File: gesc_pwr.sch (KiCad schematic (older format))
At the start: 45 parts, among them J10 PHASE_C, J11 PHASE_B, J12 NTC, J9 PHASE_A, Q1 TPH2R608NH,L1Q, Q2 TPH2R608NH,L1Q, Q3 TPH2R608NH,L1Q, Q4 TPH2R608NH,L1Q, Q5 TPH2R608NH,L1Q, Q6 TPH2R608NH,L1Q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

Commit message: save
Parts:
- J10, J11, J9: footprint gsvesc:TestPoint_Pad_5.0x5.0mm -> gesc:TestPoint_Pad_5.0x5.0mm
- J12: footprint gsvesc:2pad_smd_testpin -> gesc:2pad_smd_testpin
- Q1, Q2, Q4, Q5, Q6: footprint gsvesc:TRANS_TPHR8504PL-3PIN -> gesc:TRANS_TPHR8504PL-3PIN; symbol gsvesc:TPH2R506PL -> gesc:TPH2R506PL
- Q3: footprint gsvesc:TRANS_TPHR8504PL-3PIN -> gesc:TRANS_TPHR8504PL-3PIN; symbol gsvesc:TPH2R608NH -> gesc:TPH2R608NH
- U4, U5, U6: footprint gsvesc:INA240A1QPWRQ1 -> gesc:INA240A1QPWRQ1; symbol gsvesc:INA240A3 -> gesc:INA240A3
- U7, U8, U9: footprint gsvesc:M74VHC1GT66DTT1G -> gesc:M74VHC1GT66DTT1G; symbol gsvesc:M74VHC1GT66DTT1G -> gesc:M74VHC1GT66DTT1G
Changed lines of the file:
@@
 encoding utf-8
 Sheet 5 5
-Title "GSESC - DC Motor Controler"
-Date "2018-11-11"
-Rev "4.0"
+Title "GESC - DC Motor Controler"
+Date "2020-04-09"
+Rev "6.0"
 Comp ""
 Comment1 ""
@@
 F 0 "J10" H 4130 1642 50  0000 L CNN
 F 1 "PHASE_C" H 4130 1551 50  0000 L CNN
-F 2 "gsvesc:TestPoint_Pad_5.0x5.0mm" H 4050 1600 50  0001 C CNN
+F 2 "gesc:TestPoint_Pad_5.0x5.0mm" H 4050 1600 50  0001 C CNN
 F 3 "~" H 4050 1600 50  0001 C CNN
 	1    4050 1600
@@
 F 0 "J12" V 10054 1430 50  0000 L CNN
 F 1 "NTC" V 10145 1430 50  0000 L CNN
-F 2 "gsvesc:2pad_smd_testpin" H 10050 1350 50  0001 C CNN
+F 2 "gesc:2pad_smd_testpin" H 10050 1350 50  0001 C CNN
 F 3 "~" H 10050 1350 50  0001 C CNN
 	1    10050 1350
@@
 PHASE_C
 $Comp
-L gsvesc:M74VHC1GT66DTT1G U7
+L gesc:M74VHC1GT66DTT1G U7
 U 1 1 5DF40CC9
 P 6250 5450
 F 0 "U7" H 6900 5937 60  0000 C CNN
 F 1 "SN74LVC1G66DBVR" H 6900 5831 60  0000 C CNN
-F 2 "gsvesc:M74VHC1GT66DTT1G" H 6750 5250 60  0001 C CNN
+F 2 "gesc:M74VHC1GT66DTT1G" H 6750 5250 60  0001 C CNN
 F 3 "" H 6250 5450 60  0000 C CNN
 	1    6250 5450
@@
 CURR_B
 $Comp
-L gsvesc:M74VHC1GT66DTT1G U8
+L gesc:M74VHC1GT66DTT1G U8
 U 1 1 5DF8119A
 P 6250 3700
 F 0 "U8" H 6900 4187 60  0000 C CNN
 F 1 "SN74LVC1G66DBVR" H 6900 4081 60  0000 C CNN
-F 2 "gsvesc:M74VHC1GT66DTT1G" H 6750 3500 60  0001 C CNN
+F 2 "gesc:M74VHC1GT66DTT1G" H 6750 3500 60  0001 C CNN
 F 3 "" H 6250 3700 60  0000 C CNN
 	1    6250 3700
@@
 CURR_C
 $Comp
-L gsvesc:M74VHC1GT66DTT1G U9
+L gesc:M74VHC1GT66DTT1G U9
 U 1 1 5DFA4855
 P 6250 1950
 F 0 "U9" H 6900 2437 60  0000 C CNN
 F 1 "SN74LVC1G66DBVR" H 6900 2331 60  0000 C CNN
-F 2 "gsvesc:M74VHC1GT66DTT1G" H 6750 1750 60  0001 C CNN
+F 2 "gesc:M74VHC1GT66DTT1G" H 6750 1750 60  0001 C CNN
 F 3 "" H 6250 1950 60  0000 C CNN
 	1    6250 1950
@@
 	6150 2000 6150 2050
 $Comp
-L gsvesc:TPH2R608NH Q3
+L gesc:TPH2R608NH Q3
 U 1 1 5E3D365F
 P 1650 1300
 F 0 "Q3" H 1550 1450 50  0000 L CNN
 F 1 "TPH2R608NH,L1Q" H 1250 1150 50  0000 L CNN
-F 2 "gsvesc:TRANS_TPHR8504PL-3PIN" H 1650 1300 50  0001 C CIN
+F 2 "gesc:TRANS_TPHR8504PL-3PIN" H 1650 1300 50  0001 C CIN
 F 3 "" H 1650 1300 50  0001 L CNN
 F 4 "C146377" H 0   0   50  0001 C CNN "LCSC"
@@
 $EndComp
 $Comp
-L gsvesc:TPH2R506PL Q4
+L gesc:TPH2R506PL Q4
 U 1 1 5E3D3778
 P 1650 1950
 F 0 "Q4" H 1600 2100 50  0000 L CNN
 F 1 "TPH2R608NH,L1Q" H 1200 1800 50  0000 L CNN
-F 2 "gsvesc:TRANS_TPHR8504PL-3PIN" H 1650 1950 50  0001 C CIN
+F 2 "gesc:TRANS_TPHR8504PL-3PIN" H 1650 1950 50  0001 C CIN
 F 3 "" H 1650 1950 50  0001 L CNN
 F 4 "C146377" H 0   0   50  0001 C CNN "LCSC"
@@
 	3550 1600 3550 2050
 $Comp
-L gsvesc:INA240A3 U5
+L gesc:INA240A3 U5
 U 1 1 5E579C2A
 P 4250 2450
 F 0 "U5" H 3975 3138 60  0000 C CNN
 F 1 "INA240A2" H 3975 3032 60  0000 C CNN
-F 2 "gsvesc:INA240A1QPWRQ1" H 4000 2400 60  0001 C CNN
+F 2 "gesc:INA240A1QPWRQ1" H 4000 2400 60  0001 C CNN
 F 3 "" H 4250 2450 60  0000 C CNN
 	1    4250 2450
@@
 F 0 "J11" H 4130 3842 50  0000 L CNN
 F 1 "PHASE_B" H 4130 3751 50  0000 L CNN
-F 2 "gsvesc:TestPoint_Pad_5.0x5.0mm" H 4050 3800 50  0001 C CNN
+F 2 "gesc:TestPoint_Pad_5.0x5.0mm" H 4050 3800 50  0001 C CNN
 F 3 "~" H 4050 3800 50  0001 C CNN
 	1    4050 3800
@@
 PHASE_B
 $Comp
-L gsvesc:TPH2R506PL Q5
+L gesc:TPH2R506PL Q5
 U 1 1 5E6023E2
 P 1650 3500
 F 0 "Q5" H 1550 3650 50  0000 L CNN
 F 1 "TPH2R608NH,L1Q" H 1250 3350 50  0000 L CNN
-F 2 "gsvesc:TRANS_TPHR8504PL-3PIN" H 1650 3500 50  0001 C CIN
+F 2 "gesc:TRANS_TPHR8504PL-3PIN" H 1650 3500 50  0001 C CIN
 F 3 "" H 1650 3500 50  0001 L CNN
 F 4 "C146377" H 0   0   50  0001 C CNN "LCSC"
@@
 $EndComp
 $Comp
-L gsvesc:TPH2R506PL Q6
+L gesc:TPH2R506PL Q6
 U 1 1 5E6023E8
 P 1650 4150
 F 0 "Q6" H 1600 4300 50  0000 L CNN
 F 1 "TPH2R608NH,L1Q" H 1200 4000 50  0000 L CNN
-F 2 "gsvesc:TRANS_TPHR8504PL-3PIN" H 1650 4150 50  0001 C CIN
+F 2 "gesc:TRANS_TPHR8504PL-3PIN" H 1650 4150 50  0001 C CIN
 F 3 "" H 1650 4150 50  0001 L CNN
 F 4 "C146377" H 0   0   50  0001 C CNN "LCSC"
@@
 	3550 3800 3550 4250
 $Comp
-L gsvesc:INA240A3 U6
+L gesc:INA240A3 U6
 U 1 1 5E60242D
 P 4250 4650
 F 0 "U6" H 3975 5338 60  0000 C CNN
 F 1 "INA240A2" H 3975 5232 60  0000 C CNN
-F 2 "gsvesc:INA240A1QPWRQ1" H 4000 4600 60  0001 C CNN
+F 2 "gesc:INA240A1QPWRQ1" H 4000 4600 60  0001 C CNN
 F 3 "" H 4250 4650 60  0000 C CNN
 	1    4250 4650
@@
 F 0 "J9" H 4030 6292 50  0000 L CNN
 F 1 "PHASE_A" H 4030 6201 50  0000 L CNN
-F 2 "gsvesc:TestPoint_Pad_5.0x5.0mm" H 3950 6250 50  0001 C CNN
+F 2 "gesc:TestPoint_Pad_5.0x5.0mm" H 3950 6250 50  0001 C CNN
 F 3 "~" H 3950 6250 50  0001 C CNN
 	1    3950 6250
@@
 PHASE_A
 $Comp
-L gsvesc:TPH2R506PL Q1
+L gesc:TPH2R506PL Q1
 U 1 1 5E60A8BA
 P 1600 5950
 F 0 "Q1" H 1500 6100 50  0000 L CNN
 F 1 "TPH2R608NH,L1Q" H 1200 5800 50  0000 L CNN
-F 2 "gsvesc:TRANS_TPHR8504PL-3PIN" H 1600 5950 50  0001 C CIN
+F 2 "gesc:TRANS_TPHR8504PL-3PIN" H 1600 5950 50  0001 C CIN
 F 3 "" H 1600 5950 50  0001 L CNN
 F 4 "C146377" H 0   0   50  0001 C CNN "LCSC"
@@
 $EndComp
 $Comp
-L gsvesc:TPH2R506PL Q2
+L gesc:TPH2R506PL Q2
 U 1 1 5E60A8C0
 P 1600 6600
 F 0 "Q2" H 1550 6750 50  0000 L CNN
 F 1 "TPH2R608NH,L1Q" H 1150 6450 50  0000 L CNN
-F 2 "gsvesc:TRANS_TPHR8504PL-3PIN" H 1600 6600 50  0001 C CIN
+F 2 "gesc:TRANS_TPHR8504PL-3PIN" H 1600 6600 50  0001 C CIN
 F 3 "" H 1600 6600 50  0001 L CNN
 F 4 "C146377" H 0   0   50  0001 C CNN "LCSC"
@@
 	3450 6250 3450 6700
 $Comp
-L gsvesc:INA240A3 U4
+L gesc:INA240A3 U4
 U 1 1 5E60A905
 P 4150 7100
 F 0 "U4" H 3875 7788 60  0000 C CNN
 F 1 "INA240A2" H 3875 7682 60  0000 C CNN
-F 2 "gsvesc:INA240A1QPWRQ1" H 3900 7050 60  0001 C CNN
+F 2 "gesc:INA240A1QPWRQ1" H 3900 7050 60  0001 C CNN
 F 3 "" H 4150 7100 60  0000 C CNN
 	1    4150 7100

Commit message: save
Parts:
- added C51, C52, C53, C55, C57, C58: 10u0/75V, Capacitor_SMD:C_1210_3225Metric, symbol Device:C
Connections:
- net GND: now also C51.2, C52.2, C53.2, C55.2, C57.2, C58.2
- net VBAT: now also C51.1, C52.1, C53.1, C55.1, C57.1, C58.1
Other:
- moved on the sheet: C45, C46, C48, J10, J11, J9, R31, R45, R46, U4, U5, U6

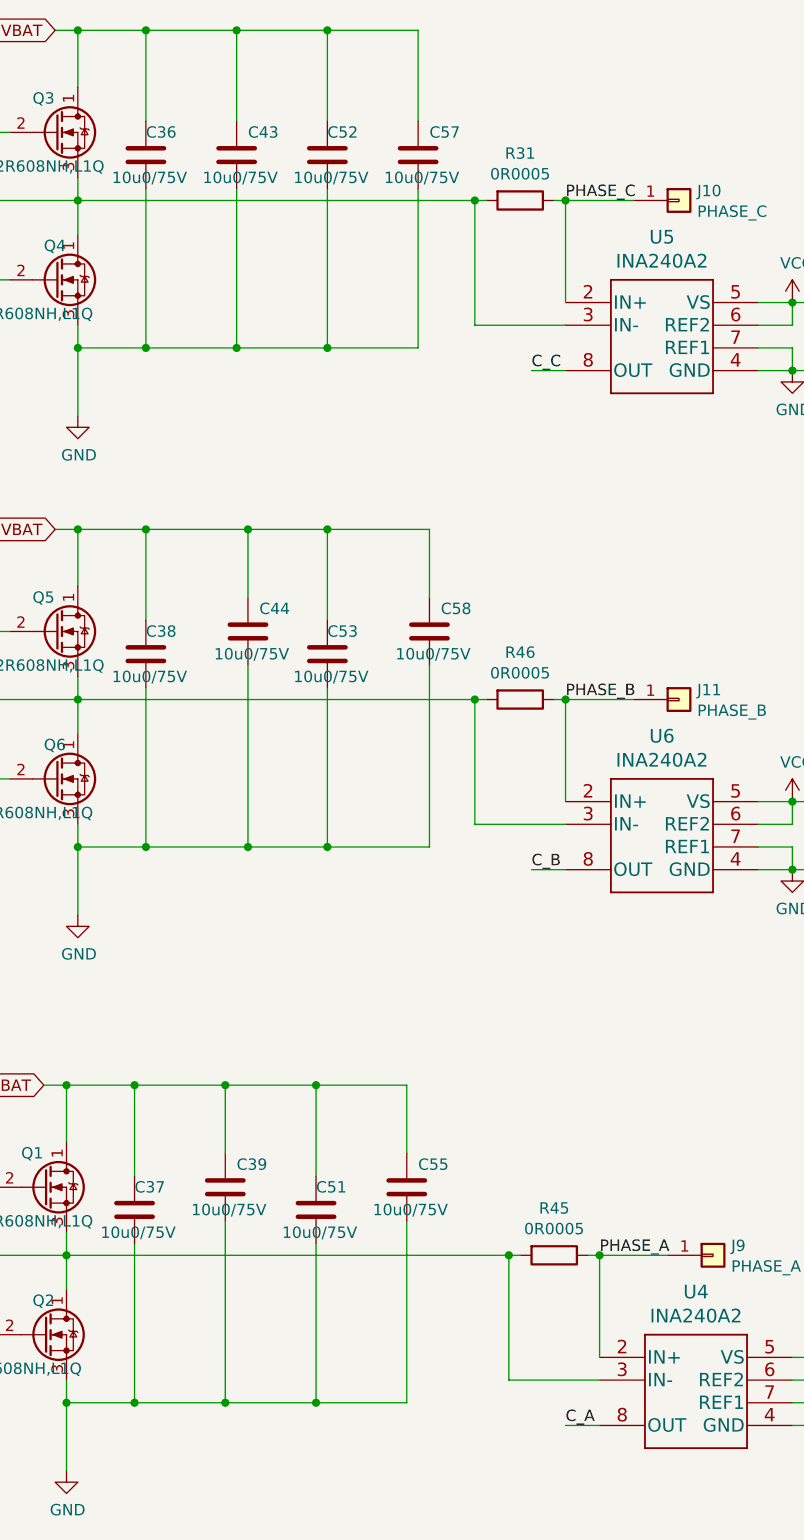
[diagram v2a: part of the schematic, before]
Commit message: PCB updated: - reroute SH_X - change 3V3 Power supply - add VBUS to 3V3 regulator - use LM5107 - change Layer/Plane assignment - move current sense tracks to layer 2
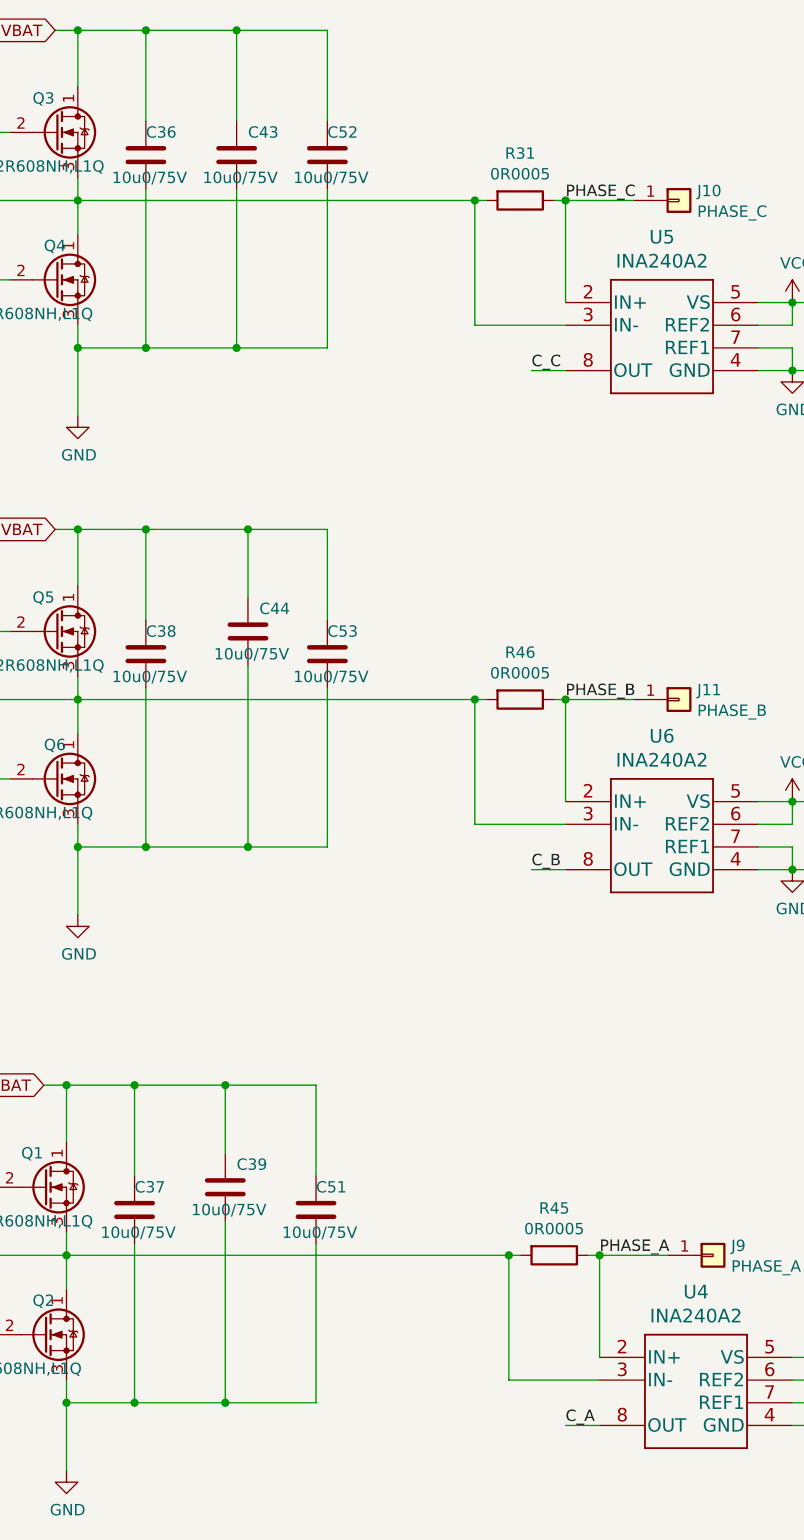
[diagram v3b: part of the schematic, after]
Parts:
- removed C55, C57, C58: 10u0/75V, Capacitor_SMD:C_1210_3225Metric, symbol Device:C
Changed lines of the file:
@@
 Wire Wire Line
 	2850 850  2850 1250
-Connection ~ 2850 850
-$Comp
-L Device:C C57
-U 1 1 601E3FDB
-P 3250 1400
-F 0 "C57" H 3300 1500 50  0000 L CNN
-F 1 "10u0/75V" H 3100 1300 50  0000 L CNN
-F 2 "Capacitor_SMD:C_1210_3225Metric" H 3288 1250 50  0001 C CNN
-F 3 "~" H 3250 1400 50  0001 C CNN
-	1    3250 1400
-	1    0    0    -1
-$EndComp
-Wire Wire Line
-	3250 850  3250 1250
-Wire Wire Line
-	2850 850  3250 850
 Wire Wire Line
 	2450 850  2850 850
@@
 Wire Wire Line
 	2450 2250 2850 2250
-Wire Wire Line
-	3250 2250 3250 1550
 Connection ~ 2450 2250
 Wire Wire Line
 	2850 1550 2850 2250
-Connection ~ 2850 2250
-Wire Wire Line
-	2850 2250 3250 2250
 Wire Wire Line
 	1750 3800 3500 3800
@@
 Wire Wire Line
 	2850 3050 2850 3450
-$Comp
-L Device:C C58
-U 1 1 6023549E
-P 3300 3500
-F 0 "C58" H 3350 3600 50  0000 L CNN
-F 1 "10u0/75V" H 3150 3400 50  0000 L CNN
-F 2 "Capacitor_SMD:C_1210_3225Metric" H 3338 3350 50  0001 C CNN
-F 3 "~" H 3300 3500 50  0001 C CNN
-	1    3300 3500
-	1    0    0    -1
-$EndComp
-Wire Wire Line
-	3300 3050 3300 3350
-Connection ~ 2850 3050
-Wire Wire Line
-	2850 3050 3300 3050
 Wire Wire Line
 	2500 3050 2850 3050
@@
 	2850 4450 2850 3750
 Connection ~ 2500 4450
-Wire Wire Line
-	2850 4450 3300 4450
-Wire Wire Line
-	3300 4450 3300 3650
-Connection ~ 2850 4450
 Wire Wire Line
 	1700 6250 3650 6250
@@
 Wire Wire Line
 	2800 5500 2800 5900
-$Comp
-L Device:C C55
-U 1 1 60289DD7
-P 3200 5950
-F 0 "C55" H 3250 6050 50  0000 L CNN
-F 1 "10u0/75V" H 3050 5850 50  0000 L CNN
-F 2 "Capacitor_SMD:C_1210_3225Metric" H 3238 5800 50  0001 C CNN
-F 3 "~" H 3200 5950 50  0001 C CNN
-	1    3200 5950
-	1    0    0    -1
-$EndComp
-Wire Wire Line
-	3200 5500 3200 5800
-Wire Wire Line
-	3200 6100 3200 6900
-Connection ~ 2800 5500
-Wire Wire Line
-	2800 5500 3200 5500
 Wire Wire Line
 	2400 5500 2800 5500
@@
 Wire Wire Line
 	2800 6200 2800 6900
-Connection ~ 2800 6900
-Wire Wire Line
-	2800 6900 3200 6900
 $EndSCHEMATC
